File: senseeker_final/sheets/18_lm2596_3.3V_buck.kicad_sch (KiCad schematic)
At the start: 9 parts, among them U5 LM2596SX-5.0/NOPB

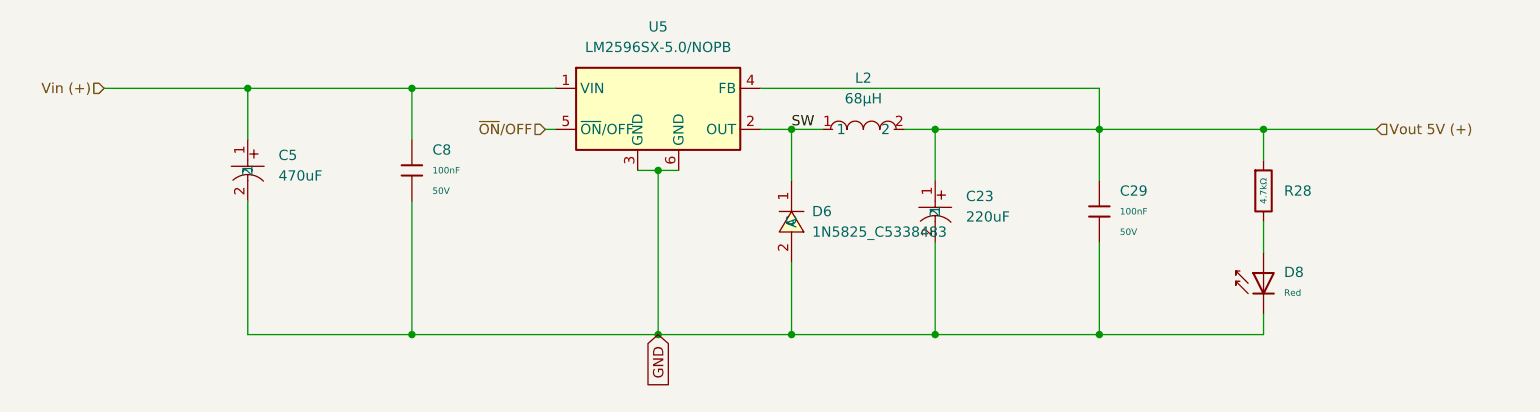
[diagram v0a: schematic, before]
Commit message: added and finished 3.3V buck
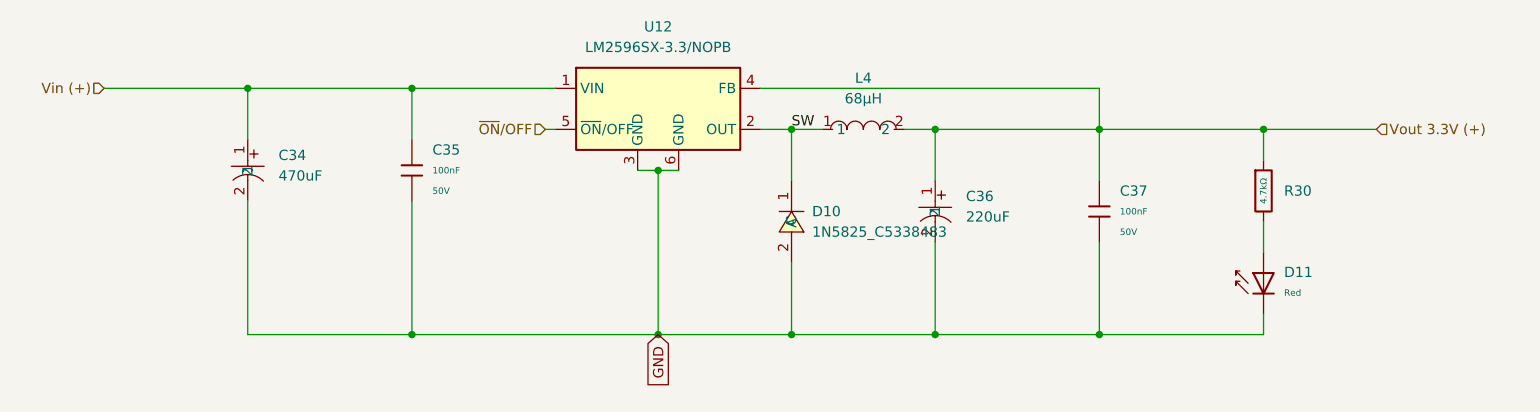
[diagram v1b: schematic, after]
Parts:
- removed U5: LM2596SX-5.0/NOPB, easyeda2kicad:TO-263-5_L10.2-W8.9-P1.70-TL, symbol easyeda2kicad:LM2596SX-5.0_NOPB
- added U12: LM2596SX-3.3/NOPB, EasyEDA:TO-263-5_L10.2-W9.9-P1.70-LS14.4-TL, symbol EasyEDA:LM2596SX-3.3_NOPB
- renumbered C5 to C34, C8 to C35, C23 to C36, C29 to C37, D6 to D10, D8 to D11, L2 to L4, R28 to R30
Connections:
- net GND: now also U12.3 (GND), U12.6 (GND)
- net SW: now also U12.2 (OUT)
- net Vin (+): now also U12.1 (VIN)
- net ~{ON}/OFF: now also U12.5 (~{ON}/OFF)
- net Vout 5V (+) renamed Vout 3.3V (+)
- net Vout 3.3V (+): now also U12.4 (FB)
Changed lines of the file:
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@@
 		)
 	)
-	(hierarchical_label "Vout 5V (+)"
+	(hierarchical_label "Vout 3.3V (+)"
 		(shape input)
 		(at 220.98 93.98 0)
@@
 		(dnp no)
 		(fields_autoplaced yes)
-		(property "Reference" "D8"
+		(property "Reference" "D11"
 			(at 209.55 111.6646 0)
 			(show_name no)
@@
 		(instances
 			(project "senseeker_final"
-				(path "/529bc8a5-ffae-43ac-972d-caccc3afab85/e6612f6f-e131-40dc-9b50-f62250179b84"
-					(reference "D8")
-					(unit 1)
-				)
-			)
-		)
-	)
-	(symbol
-		(lib_id "easyeda2kicad:LM2596SX-5.0_NOPB")
-		(at 132.08 91.44 0)
-		(unit 1)
-		(body_style 1)
-		(exclude_from_sim no)
-		(in_bom yes)
-		(on_board yes)
-		(in_pos_files yes)
-		(dnp no)
-		(fields_autoplaced yes)
-		(property "Reference" "U5"
-			(at 132.08 81.28 0)
-			(show_name no)
-			(do_not_autoplace no)
-			(effects
-				(font
-					(size 1.27 1.27)
-				)
-			)
-		)
-		(property "Value" "LM2596SX-5.0/NOPB"
-			(at 132.08 83.82 0)
-			(show_name no)
-			(do_not_autoplace no)
-			(effects
-				(font
-					(size 1.27 1.27)
-				)
-			)
-		)
-		(property "Footprint" "easyeda2kicad:TO-263-5_L10.2-W8.9-P1.70-TL"
-			(at 132.08 109.22 0)
-			(hide yes)
-			(show_name no)
-			(do_not_autoplace no)
-			(effects
-				(font
-					(size 1.27 1.27)
-				)
-			)
-		)
-		(property "Datasheet" "https://lcsc.com/product-detail/DC-DC-Converters_TI_LM2596SX-5-0-NOPB_LM2596SX-5-0-NOPB_C10002.html"
-			(at 132.08 111.76 0)
-			(hide yes)
-			(show_name no)
-			(do_not_autoplace no)
-			(effects
-				(font
-					(size 1.27 1.27)
-				)
-			)
-		)
-		(property "Description" ""
-			(at 132.08 91.44 0)
-			(hide yes)
-			(show_name no)
-			(do_not_autoplace no)
-			(effects
-				(font
-					(size 1.27 1.27)
-				)
-			)
-		)
-		(property "Manufacturer" "TI(德州仪器)"
-			(at 132.08 114.3 0)
-			(hide yes)
-			(show_name no)
-			(do_not_autoplace no)
-			(effects
-				(font
-					(size 1.27 1.27)
-				)
-			)
-		)
-		(property "MPN" "LM2596SX-5.0/NOPB"
-			(at 132.08 116.84 0)
-			(hide yes)
-			(show_name no)
-			(do_not_autoplace no)
-			(effects
-				(font
-					(size 1.27 1.27)
-				)
-			)
-		)
-		(property "LCSC Part" "C10002"
-			(at 132.08 119.38 0)
-			(hide yes)
-			(show_name no)
-			(do_not_autoplace no)
-			(effects
-				(font
-					(size 1.27 1.27)
-				)
-			)
-		)
-		(pin "2"
-		)
-		(pin "3"
-		)
-		(pin "4"
-		)
-		(pin "5"
-		)
-		(pin "1"
-		)
-		(pin "6"
-		)
-		(instances
-			(project "senseeker_final"
-				(path "/529bc8a5-ffae-43ac-972d-caccc3afab85/e6612f6f-e131-40dc-9b50-f62250179b84"
-					(reference "U5")
+				(path "/529bc8a5-ffae-43ac-972d-caccc3afab85/b4c3a0d1-ca7b-4720-8d12-20e46e9b3e38"
+					(reference "D11")
 					(unit 1)
 				)
@@
 		(dnp no)
 		(fields_autoplaced yes)
-		(property "Reference" "C5"
+		(property "Reference" "C34"
 			(at 85.09 97.1849 90)
 			(show_name no)
@@
 		(instances
 			(project "senseeker_final"
-				(path "/529bc8a5-ffae-43ac-972d-caccc3afab85/e6612f6f-e131-40dc-9b50-f62250179b84"
-					(reference "C5")
+				(path "/529bc8a5-ffae-43ac-972d-caccc3afab85/b4c3a0d1-ca7b-4720-8d12-20e46e9b3e38"
+					(reference "C34")
 					(unit 1)
 				)
@@
 		(dnp no)
 		(fields_autoplaced yes)
-		(property "Reference" "L2"
+		(property "Reference" "L4"
 			(at 157.48 87.63 0)
 			(show_name no)
@@
 		(instances
 			(project "senseeker_final"
-				(path "/529bc8a5-ffae-43ac-972d-caccc3afab85/e6612f6f-e131-40dc-9b50-f62250179b84"
-					(reference "L2")
+				(path "/529bc8a5-ffae-43ac-972d-caccc3afab85/b4c3a0d1-ca7b-4720-8d12-20e46e9b3e38"
+					(reference "L4")
 					(unit 1)
 				)
@@
 		(dnp no)
 		(fields_autoplaced yes)
-		(property "Reference" "C8"
+		(property "Reference" "C35"
 			(at 104.14 96.5199 0)
 			(show_name no)
@@
 		(instances
 			(project "senseeker_final"
-				(path "/529bc8a5-ffae-43ac-972d-caccc3afab85/e6612f6f-e131-40dc-9b50-f62250179b84"
-					(reference "C8")
+				(path "/529bc8a5-ffae-43ac-972d-caccc3afab85/b4c3a0d1-ca7b-4720-8d12-20e46e9b3e38"
+					(reference "C35")
 					(unit 1)
 				)
@@
 		(dnp no)
 		(fields_autoplaced yes)
-		(property "Reference" "D6"
+		(property "Reference" "D10"
 			(at 151.13 104.1399 90)
 			(show_name no)
@@
 		(instances
 			(project "senseeker_final"
-				(path "/529bc8a5-ffae-43ac-972d-caccc3afab85/e6612f6f-e131-40dc-9b50-f62250179b84"
-					(reference "D6")
+				(path "/529bc8a5-ffae-43ac-972d-caccc3afab85/b4c3a0d1-ca7b-4720-8d12-20e46e9b3e38"
+					(reference "D10")
 					(unit 1)
 				)
@@
 		(dnp no)
 		(fields_autoplaced yes)
-		(property "Reference" "C23"
+		(property "Reference" "C36"
 			(at 170.18 102.2649 90)
 			(show_name no)
@@
 		(instances
 			(project "senseeker_final"
-				(path "/529bc8a5-ffae-43ac-972d-caccc3afab85/e6612f6f-e131-40dc-9b50-f62250179b84"
-					(reference "C23")
+				(path "/529bc8a5-ffae-43ac-972d-caccc3afab85/b4c3a0d1-ca7b-4720-8d12-20e46e9b3e38"
+					(reference "C36")
 					(unit 1)
 				)
@@
 		(dnp no)
 		(fields_autoplaced yes)
-		(property "Reference" "C29"
+		(property "Reference" "C37"
 			(at 189.23 101.5999 0)
 			(show_name no)
@@
 		(instances
 			(project "senseeker_final"
-				(path "/529bc8a5-ffae-43ac-972d-caccc3afab85/e6612f6f-e131-40dc-9b50-f62250179b84"
-					(reference "C29")
+				(path "/529bc8a5-ffae-43ac-972d-caccc3afab85/b4c3a0d1-ca7b-4720-8d12-20e46e9b3e38"
+					(reference "C37")
+					(unit 1)
+				)
+			)
+		)
+	)
+	(symbol
+		(lib_id "EasyEDA:LM2596SX-3.3_NOPB")
+		(at 132.08 91.44 0)
+		(unit 1)
+		(body_style 1)
+		(exclude_from_sim no)
+		(in_bom yes)
+		(on_board yes)
+		(in_pos_files yes)
+		(dnp no)
+		(fields_autoplaced yes)
+		(property "Reference" "U12"
+			(at 132.08 81.28 0)
+			(show_name no)
+			(do_not_autoplace no)
+			(effects
+				(font
+					(size 1.27 1.27)
+				)
+			)
+		)
+		(property "Value" "LM2596SX-3.3/NOPB"
+			(at 132.08 83.82 0)
+			(show_name no)
+			(do_not_autoplace no)
+			(effects
+				(font
+					(size 1.27 1.27)
+				)
+			)
+		)
+		(property "Footprint" "EasyEDA:TO-263-5_L10.2-W9.9-P1.70-LS14.4-TL"
+			(at 132.08 109.22 0)
+			(hide yes)
+			(show_name no)
+			(do_not_autoplace no)
+			(effects
+				(font
+					(size 1.27 1.27)
+				)
+			)
+		)
+		(property "Datasheet" "https://lcsc.com/product-detail/DC-DC-Converters_TI_LM2596SX-3-3-NOPB_LM2596SX-3-3-NOPB_C7929.html"
+			(at 132.08 111.76 0)
+			(hide yes)
+			(show_name no)
+			(do_not_autoplace no)
+			(effects
+				(font
+					(size 1.27 1.27)
+				)
+			)
+		)
+		(property "Description" ""
+			(at 132.08 91.44 0)
+			(hide yes)
+			(show_name no)
+			(do_not_autoplace no)
+			(effects
+				(font
+					(size 1.27 1.27)
+				)
+			)
+		)
+		(property "Manufacturer" "TI(德州仪器)"
+			(at 132.08 114.3 0)
+			(hide yes)
+			(show_name no)
+			(do_not_autoplace no)
+			(effects
+				(font
+					(size 1.27 1.27)
+				)
+			)
+		)
+		(property "MPN" "LM2596SX-3.3/NOPB"
+			(at 132.08 116.84 0)
+			(hide yes)
+			(show_name no)
+			(do_not_autoplace no)
+			(effects
+				(font
+					(size 1.27 1.27)
+				)
+			)
+		)
+		(property "LCSC Part" "C7929"
+			(at 132.08 119.38 0)
+			(hide yes)
+			(show_name no)
+			(do_not_autoplace no)
+			(effects
+				(font
+					(size 1.27 1.27)
+				)
+			)
+		)
+		(pin "3"
+		)
+		(pin "4"
+		)
+		(pin "5"
+		)
+		(pin "6"
+		)
+		(pin "1"
+		)
+		(pin "2"
+		)
+		(instances
+			(project "senseeker_final"
+				(path "/529bc8a5-ffae-43ac-972d-caccc3afab85/b4c3a0d1-ca7b-4720-8d12-20e46e9b3e38"
+					(reference "U12")
 					(unit 1)
 				)
@@
 		(dnp no)
 		(fields_autoplaced yes)
-		(property "Reference" "R28"
+		(property "Reference" "R30"
 			(at 209.55 101.5999 0)
 			(show_name no)
@@
 		(instances
 			(project "senseeker_final"
-				(path "/529bc8a5-ffae-43ac-972d-caccc3afab85/e6612f6f-e131-40dc-9b50-f62250179b84"
-					(reference "R28")
+				(path "/529bc8a5-ffae-43ac-972d-caccc3afab85/b4c3a0d1-ca7b-4720-8d12-20e46e9b3e38"
+					(reference "R30")
 					(unit 1)
 				)
